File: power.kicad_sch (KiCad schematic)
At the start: 12 parts, among them U8 LM2940S-5.0/NOPB

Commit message: Populate Board
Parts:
- removed C19: 22uF, Capacitor_SMD:C_0805_2012Metric_Pad1.15x1.40mm_HandSolder, symbol Device:C
- removed R45: 10k, Resistor_SMD:R_0805_2012Metric, symbol Device:R
- removed R46: 120R, Resistor_SMD:R_0805_2012Metric, symbol Device:R
- removed S1: AYZ0202AGRLC, AYZ0202AGRLC, symbol Misc:AYZ0202AGRLC
- added C24: 10µ, Capacitor_SMD:C_0805_2012Metric, symbol Device:C
- added C25, C26, C27, C28, C29, C30: 100n, Capacitor_SMD:C_0805_2012Metric, symbol Device:C
- added C31: 10n, Capacitor_SMD:C_0805_2012Metric, symbol Device:C
- added C32, C33: 1µ, Capacitor_SMD:C_0805_2012Metric, symbol Device:C
- added C34: C, Capacitor_SMD:C_0805_2012Metric, symbol Device:C
- added FB1: 120R, Inductor_SMD:L_0805_2012Metric, symbol Device:FerriteBead
- added J6: Screw_Terminal_01x02, TerminalBlock:TerminalBlock_bornier-2_P5.08mm, symbol Connector:Screw_Terminal_01x02
- added R83, R84, R85: 10k, Resistor_SMD:R_0805_2012Metric, symbol Device:R
- added SW1, SW2: SW_DIP_x01, Button_Switch_SMD:SW_SPST_B3U-1000P, symbol Switch:SW_DIP_x01
- added SW3: SW_SPDT, Button_Switch_SMD:SW_SPDT_CK_JS102011SAQN, symbol Switch:SW_SPDT
- C35: renamed from C17; Voltage 35v -> 50v
- F1: Digikey Part Number 507-1361-1-ND -> (none); Manufacturer_Name Bel Fuse -> (none); Manufacturer_Part_Number 0ZCC0050FF2C -> (none); URL https://www.digikey.com.au/product-detail/en/bel-fuse-inc/0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 -> (none)
- U18: renamed from U8; footprint Package_TO_SOT_SMD:TO-263-3_TabPin2 -> IC_Automotive:TO-263-3_TabPin2-Clean
- renumbered C18 to C36, C20 to C37, C21 to C38, D15 to D20, D14 to D21
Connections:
- net GND: now also C24.2, C25.2, C26.2, C27.2, C28.2, C29.2, C30.2, C31.2, C32.2, C33.2, C34.2, J6.2 (Pin_2), R85.2, SW1.2
- net 12V-SW renamed +12V
- net +12V: now also J6.1 (Pin_1)
- net VDD renamed 5V-REGULATOR
- net 5V-REGULATOR: now also SW3.1 (A); no longer F1.2
- net VDDA renamed +5V
- net +5V: now also SW3.2 (B)
- net VRegIn: no longer names the net of C35.1, C36.1, D20.1 (K), D21.1 (K), U18.1 (VI)
- new net: R84.2, R85.1, SW2.1
- new net: R83.2, SW1.1
- new net +3.3V: C24.1, C25.1, C26.1, C27.1, C28.1, C29.1, C30.1, C31.1, C32.1, FB1.1, SW2.2
- new net +3.3VA: C33.1, FB1.2
- new net +5VA: F1.2
- new net 5V-USB: SW3.3 (C)
- new net MCU_BOOT: R84.1
- new net MCU_RESET: C34.1, R83.1
- no-connect marks 5 -> 0
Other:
- note added: "5V Source Selector"
- note added: "External 12V Connnector"
- note added: "Power Regulator (12V-5V)"
- note added: "STM32 3.3V Decoupling"
- note added: "STM32 3.3VA Decoupling"
- note added: "STM32 Boot"
- note added: "STM32 Reset"
- note removed: "Power Regulator"
- note removed: "Refer AVR040 Application Note"
- note removed: "Reset Protection"
- moved on the sheet: C35, C36, C37, C38, D20, D21, U18

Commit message: Pre MCU switch
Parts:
- added C41: 100n, Capacitor_SMD:C_0805_2012Metric, symbol Device:C
- added C42, C43: 2.2µ, Capacitor_SMD:C_0805_2012Metric, symbol Device:C
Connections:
- net +12V: no longer J6.1 (Pin_1)
- net +3.3V: now also C41.1, C42.1, C43.1
- net GND: now also C41.2, C42.2, C43.2
- new net RAW-BAT: J6.1 (Pin_1)
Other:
- note added: "STM32 VCAP Decoupling"

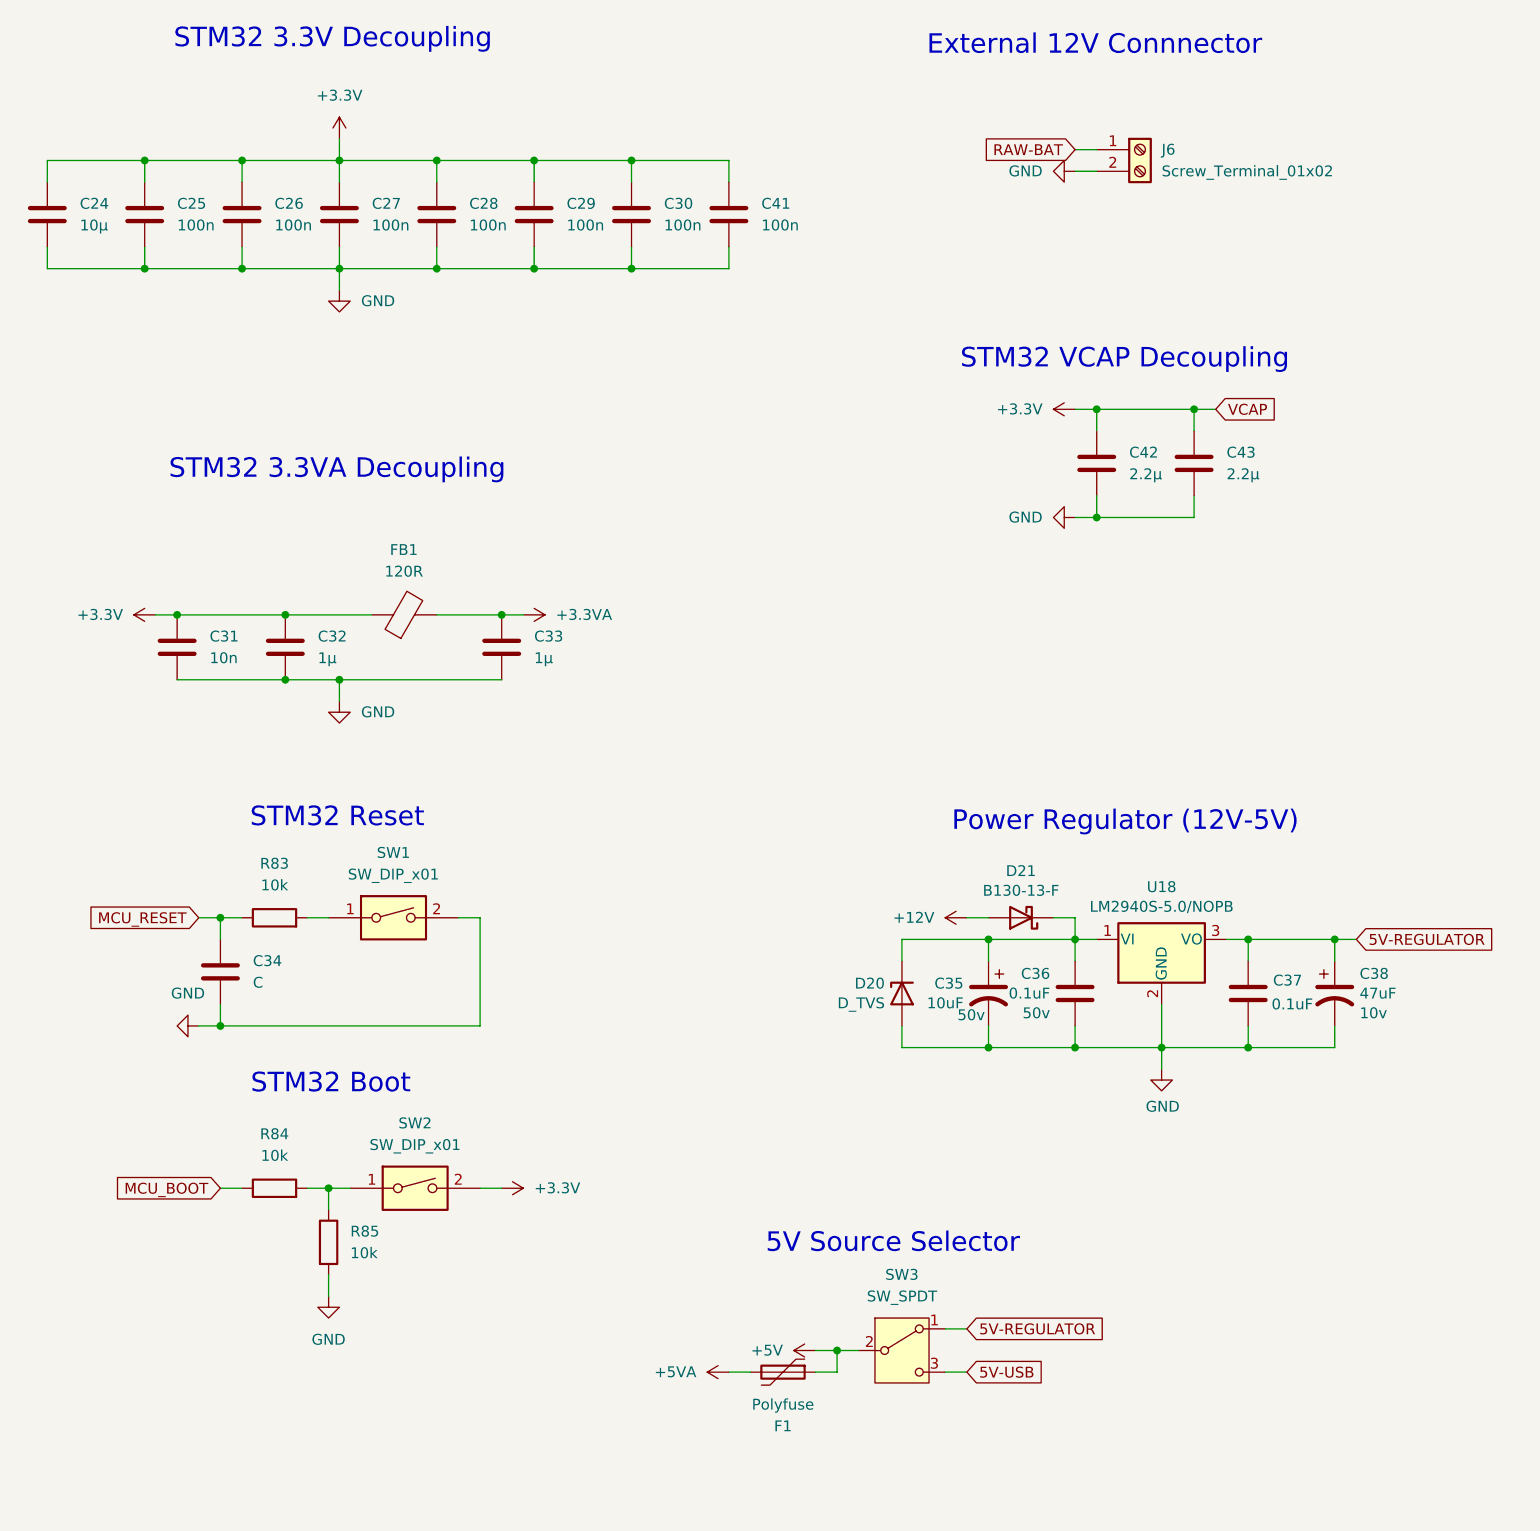
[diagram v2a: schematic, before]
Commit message: Fix MCU decoupling capacitors
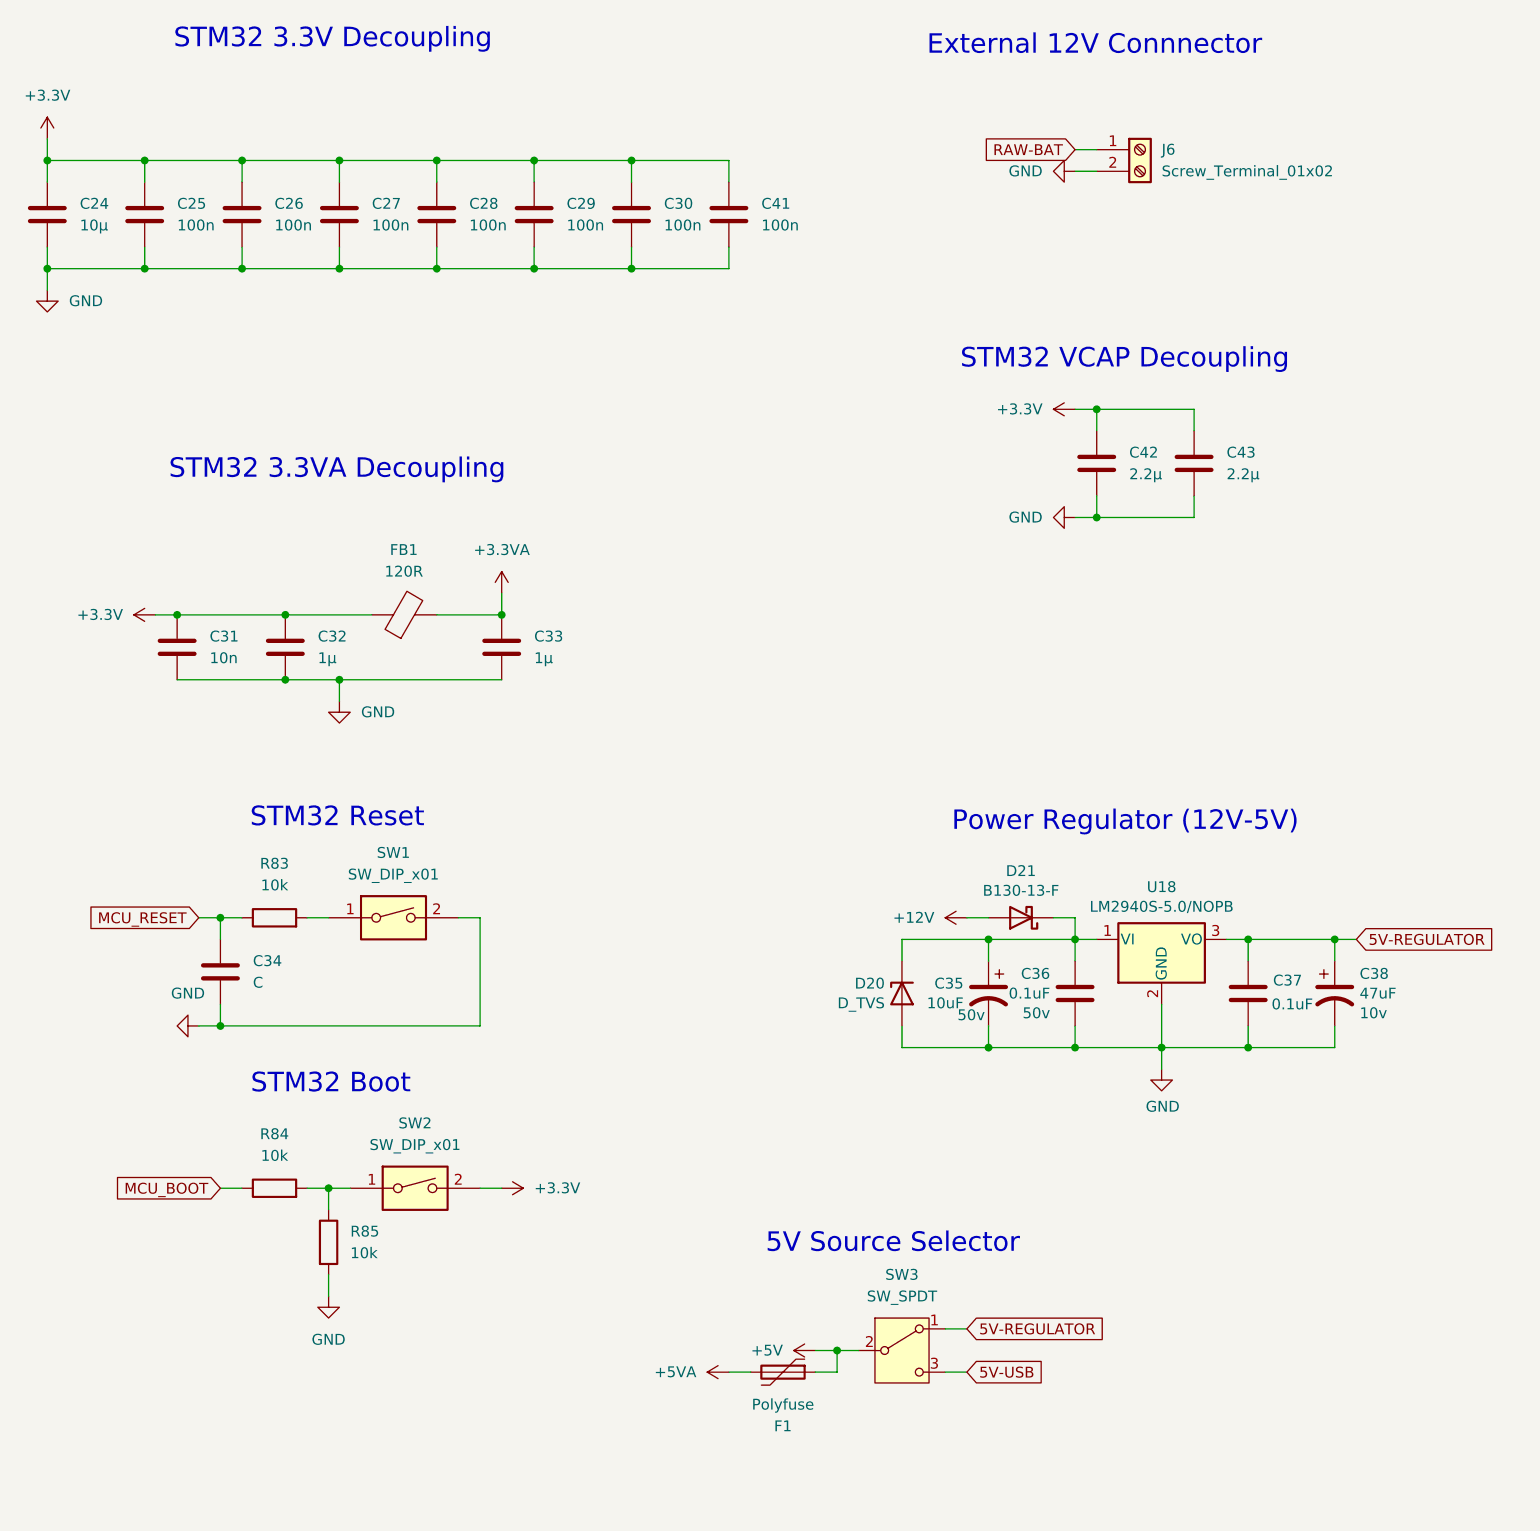
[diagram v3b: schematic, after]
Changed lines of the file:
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@@
 	)
 	(junction
-		(at 158.75 67.31)
-		(diameter 0)
-		(color 0 0 0 0)
-	)
-	(junction
 		(at 81.28 50.8)
 		(diameter 0)
@@
 	)
 	(junction
+		(at 24.13 50.8)
+		(diameter 0)
+		(color 0 0 0 0)
+	)
+	(junction
 		(at 44.45 139.7)
 		(diameter 0)
@@
 	)
 	(junction
+		(at 24.13 38.1)
+		(diameter 0)
+		(color 0 0 0 0)
+	)
+	(junction
 		(at 58.42 50.8)
 		(diameter 0)
@@
 	(wire
 		(pts
-			(xy 144.78 127) (xy 144.78 129.54)
+			(xy 24.13 35.56) (xy 24.13 38.1)
 		)
 		(stroke
@@
 	(wire
 		(pts
-			(xy 158.75 67.31) (xy 161.29 67.31)
+			(xy 144.78 127) (xy 144.78 129.54)
 		)
 		(stroke
@@
 	(wire
 		(pts
-			(xy 58.42 35.56) (xy 58.42 38.1)
+			(xy 77.47 88.9) (xy 77.47 91.44)
 		)
 		(stroke
@@
 	(wire
 		(pts
-			(xy 77.47 91.44) (xy 80.01 91.44)
-		)
-		(stroke
-			(width 0)
-			(type default)
-		)
-	)
-	(wire
-		(pts
 			(xy 81.28 38.1) (xy 92.71 38.1)
 		)
@@
 	(wire
 		(pts
-			(xy 58.42 50.8) (xy 58.42 53.34)
-		)
-		(stroke
-			(width 0)
-			(type default)
-		)
-	)
-	(wire
-		(pts
 			(xy 69.85 48.26) (xy 69.85 50.8)
 		)
@@
 	(wire
 		(pts
+			(xy 24.13 50.8) (xy 24.13 53.34)
+		)
+		(stroke
+			(width 0)
+			(type default)
+		)
+	)
+	(wire
+		(pts
 			(xy 46.99 40.64) (xy 46.99 38.1)
 		)
@@
 		)
 	)
-	(global_label "VCAP"
-		(shape input)
-		(at 161.29 67.31 0)
-		(fields_autoplaced yes)
-		(effects
-			(font
-				(size 1.27 1.27)
-			)
-			(justify left)
-		)
-		(property "Intersheetrefs" "${INTERSHEET_REFS}"
-			(at 168.3382 67.31 0)
-			(effects
-				(font
-					(size 1.27 1.27)
-				)
-				(justify left)
-				(hide yes)
-			)
-		)
-	)
 	(global_label "MCU_RESET"
 		(shape input)
@@
 	)
 	(symbol
+		(lib_id "power:+3.3VA")
+		(at 77.47 88.9 0)
+		(unit 1)
+		(exclude_from_sim no)
+		(in_bom yes)
+		(on_board yes)
+		(dnp no)
+		(fields_autoplaced yes)
+		(property "Reference" "#PWR02"
+			(at 77.47 92.71 0)
+			(effects
+				(font
+					(size 1.27 1.27)
+				)
+				(hide yes)
+			)
+		)
+		(property "Value" "+3.3VA"
+			(at 77.47 83.82 0)
+			(effects
+				(font
+					(size 1.27 1.27)
+				)
+			)
+		)
+		(property "Footprint" ""
+			(at 77.47 88.9 0)
+			(effects
+				(font
+					(size 1.27 1.27)
+				)
+				(hide yes)
+			)
+		)
+		(property "Datasheet" ""
+			(at 77.47 88.9 0)
+			(effects
+				(font
+					(size 1.27 1.27)
+				)
+				(hide yes)
+			)
+		)
+		(property "Description" "Power symbol creates a global label with name \"+3.3VA\""
+			(at 77.47 88.9 0)
+			(effects
+				(font
+					(size 1.27 1.27)
+				)
+				(hide yes)
+			)
+		)
+		(pin "1"
+		)
+		(instances
+			(project ""
+				(path "/5a477c6c-8a44-40c8-a075-f8fcd765b0eb/00000000-0000-0000-0000-00005cd18ec3"
+					(reference "#PWR02")
+					(unit 1)
+				)
+			)
+		)
+	)
+	(symbol
 		(lib_id "power:+12V")
 		(at 132.08 127 90)
@@
 	)
 	(symbol
-		(lib_id "power:+3.3VA")
-		(at 80.01 91.44 270)
-		(unit 1)
-		(exclude_from_sim no)
-		(in_bom yes)
-		(on_board yes)
-		(dnp no)
-		(fields_autoplaced yes)
-		(property "Reference" "#PWR0207"
-			(at 76.2 91.44 0)
-			(effects
-				(font
-					(size 1.27 1.27)
-				)
-				(hide yes)
-			)
-		)
-		(property "Value" "+3.3VA"
-			(at 83.82 91.4399 90)
-			(effects
-				(font
-					(size 1.27 1.27)
-				)
-				(justify left)
-			)
-		)
-		(property "Footprint" ""
-			(at 80.01 91.44 0)
-			(effects
-				(font
-					(size 1.27 1.27)
-				)
-				(hide yes)
-			)
-		)
-		(property "Datasheet" ""
-			(at 80.01 91.44 0)
-			(effects
-				(font
-					(size 1.27 1.27)
-				)
-				(hide yes)
-			)
-		)
-		(property "Description" "Power symbol creates a global label with name \"+3.3VA\""
-			(at 80.01 91.44 0)
-			(effects
-				(font
-					(size 1.27 1.27)
-				)
-				(hide yes)
-			)
-		)
-		(pin "1"
-		)
-		(instances
-			(project ""
-				(path "/5a477c6c-8a44-40c8-a075-f8fcd765b0eb/00000000-0000-0000-0000-00005cd18ec3"
-					(reference "#PWR0207")
-					(unit 1)
-				)
-			)
-		)
-	)
-	(symbol
 		(lib_id "power:+3.3V")
 		(at 77.47 158.75 270)
@@
 	(symbol
 		(lib_id "power:GND")
-		(at 58.42 53.34 0)
+		(at 24.13 53.34 0)
 		(unit 1)
 		(exclude_from_sim no)
@@
 		(fields_autoplaced yes)
 		(property "Reference" "#PWR0201"
-			(at 58.42 59.69 0)
+			(at 24.13 59.69 0)
 			(effects
 				(font
@@
 		)
 		(property "Value" "GND"
-			(at 60.96 54.6099 0)
+			(at 26.67 54.6099 0)
 			(effects
 				(font
@@
 		)
 		(property "Footprint" ""
-			(at 58.42 53.34 0)
+			(at 24.13 53.34 0)
 			(effects
 				(font
@@
 		)
 		(property "Datasheet" ""
-			(at 58.42 53.34 0)
+			(at 24.13 53.34 0)
 			(effects
 				(font
@@
 		)
 		(property "Description" "Power symbol creates a global label with name \"GND\" , ground"
-			(at 58.42 53.34 0)
+			(at 24.13 53.34 0)
 			(effects
 				(font
@@
 	(symbol
 		(lib_id "power:+3.3V")
-		(at 58.42 35.56 0)
+		(at 24.13 35.56 0)
 		(unit 1)
 		(exclude_from_sim no)
@@
 		(fields_autoplaced yes)
 		(property "Reference" "#PWR0200"
-			(at 58.42 39.37 0)
+			(at 24.13 39.37 0)
 			(effects
 				(font
@@
 		)
 		(property "Value" "+3.3V"
-			(at 58.42 30.48 0)
+			(at 24.13 30.48 0)
 			(effects
 				(font
@@
 		)
 		(property "Footprint" ""
-			(at 58.42 35.56 0)
+			(at 24.13 35.56 0)
 			(effects
 				(font
@@
 		)
 		(property "Datasheet" ""
-			(at 58.42 35.56 0)
+			(at 24.13 35.56 0)
 			(effects
 				(font
@@
 		)
 		(property "Description" "Power symbol creates a global label with name \"+3.3V\""
-			(at 58.42 35.56 0)
+			(at 24.13 35.56 0)
 			(effects
 				(font
